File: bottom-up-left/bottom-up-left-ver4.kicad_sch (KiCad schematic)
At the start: 111 parts, among them U1 ProMicro, U2 PJ-320A

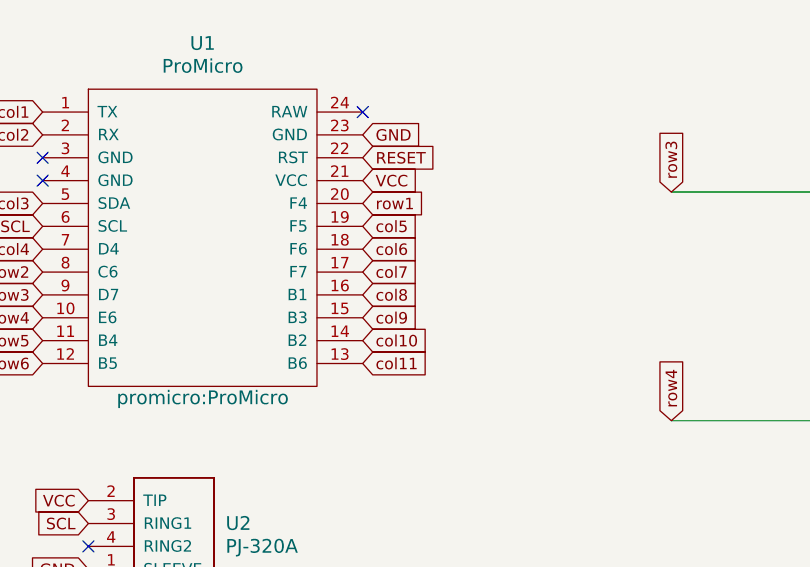
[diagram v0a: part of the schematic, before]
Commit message: Fix: relocated left PCB wire more tight
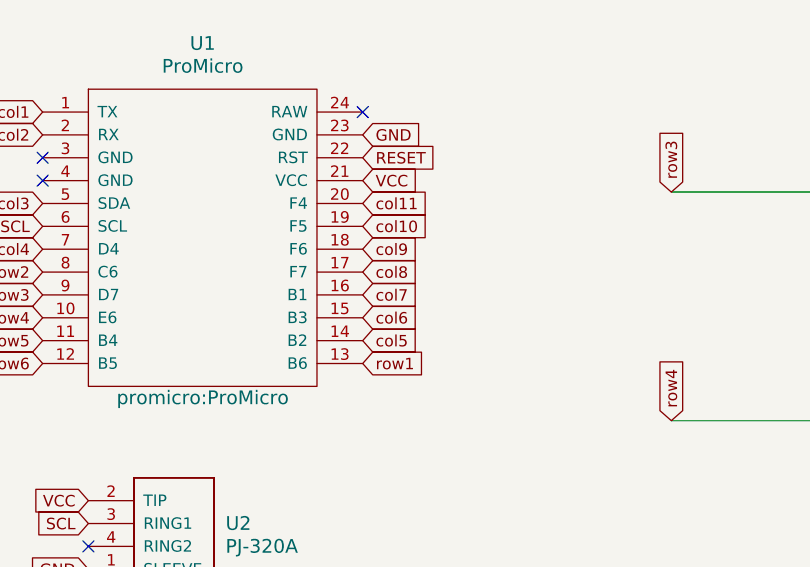
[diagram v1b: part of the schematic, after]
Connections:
- net col10: now also U1.19 (F5); no longer U1.14 (B2)
- net col11: now also U1.20 (F4); no longer U1.13 (B6)
- net col5: now also U1.14 (B2); no longer U1.19 (F5)
- net col6: now also U1.15 (B3); no longer U1.18 (F6)
- net col7: now also U1.16 (B1); no longer U1.17 (F7)
- net col8: now also U1.17 (F7); no longer U1.16 (B1)
- net col9: now also U1.18 (F6); no longer U1.15 (B3)
- net row1: now also U1.13 (B6); no longer U1.20 (F4)
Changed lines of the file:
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@@
     )
   )
-  (global_label "col7" (shape input) (at 87.63 158.75 0) (fields_autoplaced)
+  (global_label "col7" (shape input) (at 87.63 161.29 0) (fields_autoplaced)
+    (effects (font (size 1.27 1.27)) (justify left))
+    (property "Intersheetrefs" "${INTERSHEET_REFS}" (at 94.6481 161.29 0)
+      (effects (font (size 1.27 1.27)) (justify left) hide)
+    )
+  )
+  (global_label "GND" (shape input) (at 68.58 209.55 0)
+    (effects (font (size 1.27 1.27)) (justify left))
+    (property "Intersheetrefs" "${INTERSHEET_REFS}" (at 68.58 209.55 0)
+      (effects (font (size 1.27 1.27)) hide)
+    )
+  )
+  (global_label "SCL" (shape input) (at 52.07 153.67 180)
+    (effects (font (size 1.27 1.27)) (justify right))
+    (property "Intersheetrefs" "${INTERSHEET_REFS}" (at 52.07 153.67 0)
+      (effects (font (size 1.27 1.27)) hide)
+    )
+  )
+  (global_label "row3" (shape input) (at 52.07 161.29 180)
+    (effects (font (size 1.27 1.27)) (justify right))
+    (property "Intersheetrefs" "${INTERSHEET_REFS}" (at 52.07 161.29 0)
+      (effects (font (size 1.27 1.27)) hide)
+    )
+  )
+  (global_label "col5" (shape input) (at 87.63 166.37 0) (fields_autoplaced)
+    (effects (font (size 1.27 1.27)) (justify left))
+    (property "Intersheetrefs" "${INTERSHEET_REFS}" (at 94.6481 166.37 0)
+      (effects (font (size 1.27 1.27)) (justify left) hide)
+    )
+  )
+  (global_label "col9" (shape input) (at 287.02 60.96 0) (fields_autoplaced)
+    (effects (font (size 1.27 1.27)) (justify left))
+    (property "Intersheetrefs" "${INTERSHEET_REFS}" (at 294.0381 60.96 0)
+      (effects (font (size 1.27 1.27)) (justify left) hide)
+    )
+  )
+  (global_label "row3" (shape input) (at 121.92 149.86 90)
+    (effects (font (size 1.27 1.27)) (justify left))
+    (property "Intersheetrefs" "${INTERSHEET_REFS}" (at 121.92 149.86 0)
+      (effects (font (size 1.27 1.27)) hide)
+    )
+  )
+  (global_label "row1" (shape input) (at 87.63 168.91 0)
+    (effects (font (size 1.27 1.27)) (justify left))
+    (property "Intersheetrefs" "${INTERSHEET_REFS}" (at 87.63 168.91 0)
+      (effects (font (size 1.27 1.27)) hide)
+    )
+  )
+  (global_label "col7" (shape input) (at 261.62 60.96 0) (fields_autoplaced)
+    (effects (font (size 1.27 1.27)) (justify left))
+    (property "Intersheetrefs" "${INTERSHEET_REFS}" (at 268.6381 60.96 0)
+      (effects (font (size 1.27 1.27)) (justify left) hide)
+    )
+  )
+  (global_label "col8" (shape input) (at 274.32 60.96 0) (fields_autoplaced)
+    (effects (font (size 1.27 1.27)) (justify left))
+    (property "Intersheetrefs" "${INTERSHEET_REFS}" (at 281.3381 60.96 0)
+      (effects (font (size 1.27 1.27)) (justify left) hide)
+    )
+  )
+  (global_label "col10" (shape input) (at 299.72 60.96 0) (fields_autoplaced)
+    (effects (font (size 1.27 1.27)) (justify left))
+    (property "Intersheetrefs" "${INTERSHEET_REFS}" (at 307.9476 60.96 0)
+      (effects (font (size 1.27 1.27)) (justify left) hide)
+    )
+  )
+  (global_label "GND" (shape input) (at 87.63 143.51 0)
+    (effects (font (size 1.27 1.27)) (justify left))
+    (property "Intersheetrefs" "${INTERSHEET_REFS}" (at 87.63 143.51 0)
+      (effects (font (size 1.27 1.27)) hide)
+    )
+  )
+  (global_label "col8" (shape input) (at 87.63 158.75 0) (fields_autoplaced)
     (effects (font (size 1.27 1.27)) (justify left))
     (property "Intersheetrefs" "${INTERSHEET_REFS}" (at 94.6481 158.75 0)
@@
     )
   )
-  (global_label "GND" (shape input) (at 68.58 209.55 0)
-    (effects (font (size 1.27 1.27)) (justify left))
-    (property "Intersheetrefs" "${INTERSHEET_REFS}" (at 68.58 209.55 0)
-      (effects (font (size 1.27 1.27)) hide)
-    )
-  )
-  (global_label "SCL" (shape input) (at 52.07 153.67 180)
-    (effects (font (size 1.27 1.27)) (justify right))
-    (property "Intersheetrefs" "${INTERSHEET_REFS}" (at 52.07 153.67 0)
-      (effects (font (size 1.27 1.27)) hide)
-    )
-  )
-  (global_label "row3" (shape input) (at 52.07 161.29 180)
-    (effects (font (size 1.27 1.27)) (justify right))
-    (property "Intersheetrefs" "${INTERSHEET_REFS}" (at 52.07 161.29 0)
-      (effects (font (size 1.27 1.27)) hide)
-    )
-  )
-  (global_label "col5" (shape input) (at 87.63 153.67 0) (fields_autoplaced)
-    (effects (font (size 1.27 1.27)) (justify left))
-    (property "Intersheetrefs" "${INTERSHEET_REFS}" (at 94.6481 153.67 0)
-      (effects (font (size 1.27 1.27)) (justify left) hide)
-    )
-  )
-  (global_label "col9" (shape input) (at 287.02 60.96 0) (fields_autoplaced)
-    (effects (font (size 1.27 1.27)) (justify left))
-    (property "Intersheetrefs" "${INTERSHEET_REFS}" (at 294.0381 60.96 0)
-      (effects (font (size 1.27 1.27)) (justify left) hide)
-    )
-  )
-  (global_label "row3" (shape input) (at 121.92 149.86 90)
-    (effects (font (size 1.27 1.27)) (justify left))
-    (property "Intersheetrefs" "${INTERSHEET_REFS}" (at 121.92 149.86 0)
-      (effects (font (size 1.27 1.27)) hide)
-    )
-  )
-  (global_label "row1" (shape input) (at 87.63 151.13 0)
-    (effects (font (size 1.27 1.27)) (justify left))
-    (property "Intersheetrefs" "${INTERSHEET_REFS}" (at 87.63 151.13 0)
-      (effects (font (size 1.27 1.27)) hide)
-    )
-  )
-  (global_label "col7" (shape input) (at 261.62 60.96 0) (fields_autoplaced)
-    (effects (font (size 1.27 1.27)) (justify left))
-    (property "Intersheetrefs" "${INTERSHEET_REFS}" (at 268.6381 60.96 0)
-      (effects (font (size 1.27 1.27)) (justify left) hide)
-    )
-  )
-  (global_label "col8" (shape input) (at 274.32 60.96 0) (fields_autoplaced)
-    (effects (font (size 1.27 1.27)) (justify left))
-    (property "Intersheetrefs" "${INTERSHEET_REFS}" (at 281.3381 60.96 0)
-      (effects (font (size 1.27 1.27)) (justify left) hide)
-    )
-  )
-  (global_label "col10" (shape input) (at 299.72 60.96 0) (fields_autoplaced)
-    (effects (font (size 1.27 1.27)) (justify left))
-    (property "Intersheetrefs" "${INTERSHEET_REFS}" (at 307.9476 60.96 0)
-      (effects (font (size 1.27 1.27)) (justify left) hide)
-    )
-  )
-  (global_label "GND" (shape input) (at 87.63 143.51 0)
-    (effects (font (size 1.27 1.27)) (justify left))
-    (property "Intersheetrefs" "${INTERSHEET_REFS}" (at 87.63 143.51 0)
-      (effects (font (size 1.27 1.27)) hide)
-    )
-  )
-  (global_label "col8" (shape input) (at 87.63 161.29 0) (fields_autoplaced)
-    (effects (font (size 1.27 1.27)) (justify left))
-    (property "Intersheetrefs" "${INTERSHEET_REFS}" (at 94.6481 161.29 0)
-      (effects (font (size 1.27 1.27)) (justify left) hide)
-    )
-  )
   (global_label "row2" (shape input) (at 121.92 124.46 90)
     (effects (font (size 1.27 1.27)) (justify left))
@@
     )
   )
-  (global_label "col6" (shape input) (at 87.63 156.21 0) (fields_autoplaced)
-    (effects (font (size 1.27 1.27)) (justify left))
-    (property "Intersheetrefs" "${INTERSHEET_REFS}" (at 94.6481 156.21 0)
+  (global_label "col6" (shape input) (at 87.63 163.83 0) (fields_autoplaced)
+    (effects (font (size 1.27 1.27)) (justify left))
+    (property "Intersheetrefs" "${INTERSHEET_REFS}" (at 94.6481 163.83 0)
       (effects (font (size 1.27 1.27)) (justify left) hide)
     )
@@
     )
   )
-  (global_label "col9" (shape input) (at 87.63 163.83 0) (fields_autoplaced)
-    (effects (font (size 1.27 1.27)) (justify left))
-    (property "Intersheetrefs" "${INTERSHEET_REFS}" (at 94.6481 163.83 0)
+  (global_label "col9" (shape input) (at 87.63 156.21 0) (fields_autoplaced)
+    (effects (font (size 1.27 1.27)) (justify left))
+    (property "Intersheetrefs" "${INTERSHEET_REFS}" (at 94.6481 156.21 0)
       (effects (font (size 1.27 1.27)) (justify left) hide)
     )
@@
     )
   )
-  (global_label "col11" (shape input) (at 87.63 168.91 0) (fields_autoplaced)
-    (effects (font (size 1.27 1.27)) (justify left))
-    (property "Intersheetrefs" "${INTERSHEET_REFS}" (at 95.8576 168.91 0)
+  (global_label "col11" (shape input) (at 87.63 151.13 0) (fields_autoplaced)
+    (effects (font (size 1.27 1.27)) (justify left))
+    (property "Intersheetrefs" "${INTERSHEET_REFS}" (at 95.8576 151.13 0)
       (effects (font (size 1.27 1.27)) (justify left) hide)
     )
@@
     )
   )
-  (global_label "col10" (shape input) (at 87.63 166.37 0) (fields_autoplaced)
-    (effects (font (size 1.27 1.27)) (justify left))
-    (property "Intersheetrefs" "${INTERSHEET_REFS}" (at 95.8576 166.37 0)
-      (effects (font (size 1.27 1.27)) (justify left) hide)
-    )
+  (global_label "col10" (shape input) (at 87.63 153.67 0) (fields_autoplaced)
+    (effects (font (size 1.27 1.27)) (justify left))
+    (property "Intersheetrefs" "${INTERSHEET_REFS}" (at 95.8576 153.67 0)
+      (effects (font (size 1.27 1.27)) (justify left) hide)
+    )
